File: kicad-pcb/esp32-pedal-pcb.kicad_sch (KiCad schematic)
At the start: 42 parts, among them J1 USB_C_Receptacle_USB2.0_14P, Q1 Q_PMOS_GSD, U1 MCP73871, U2 TLV75733PDBV, U3 ESP32-S3-WROOM-1, U4 TPD2EUSB30, U5 TPD2E2U06DCK, U6 TPS2553DBVR

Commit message: Update PCB schematic
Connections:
- net GND: now also D2.2 (A2); no longer D2.1 (A1)
- net VBUS PROTECTED: now also D2.1 (A1); no longer D2.2 (A2)
- net BAT SWITCHED renamed 5V SWITCHED
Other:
- moved on the sheet: D2
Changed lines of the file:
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@@
 	)
 	(junction
+		(at 90.17 74.93)
+		(diameter 0)
+		(color 0 0 0 0)
+	)
+	(junction
 		(at 152.4 144.78)
 		(diameter 0)
@@
 	)
 	(junction
-		(at 90.17 74.93)
-		(diameter 0)
-		(color 0 0 0 0)
-	)
-	(junction
 		(at 167.64 116.84)
 		(diameter 0)
@@
 	(wire
 		(pts
-			(xy 90.17 74.93) (xy 93.98 74.93)
-		)
-		(stroke
-			(width 0)
-			(type default)
-		)
-	)
-	(wire
-		(pts
 			(xy 97.79 58.42) (xy 71.12 58.42)
 		)
@@
 	(wire
 		(pts
+			(xy 90.17 74.93) (xy 93.98 74.93)
+		)
+		(stroke
+			(width 0)
+			(type default)
+		)
+	)
+	(wire
+		(pts
 			(xy 265.43 214.63) (xy 265.43 227.33)
 		)
@@
 		)
 	)
-	(label "BAT SWITCHED"
+	(label "5V SWITCHED"
 		(at 182.88 85.09 0)
 		(effects
@@
 	(symbol
 		(lib_id "Diode:SMF5V0A")
-		(at 90.17 78.74 90)
+		(at 90.17 78.74 270)
 		(unit 1)
 		(exclude_from_sim no)
@@
 					(size 1.27 1.27)
 				)
-				(justify right)
+				(justify left)
 			)
 		)
@@
 					(size 1.27 1.27)
 				)
-				(justify right)
+				(justify left)
 			)
 		)
 		(property "Footprint" "Diode_SMD:D_SMF"
-			(at 95.25 78.74 0)
+			(at 85.09 78.74 0)
 			(effects
 				(font
@@
 		)
 		(property "Datasheet" "https://www.vishay.com/doc?85881"
-			(at 90.17 80.01 0)
+			(at 90.17 77.47 0)
 			(effects
 				(font

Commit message: Update PCB schematic
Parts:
- removed C1: 0.1µF, Capacitor_SMD:C_0805_2012Metric, symbol Device:C_Small_US
- removed C2: 1µF, Capacitor_SMD:C_0805_2012Metric, symbol Device:C_US
- removed C3: 47µF, Capacitor_SMD:C_0805_2012Metric, symbol Device:C_US
- removed C4: 100µF, Capacitor_SMD:C_0805_2012Metric, symbol Device:C_US
- removed C5: 0.1µF, Capacitor_SMD:C_0805_2012Metric, symbol Device:C_US
- removed C6: 1µF, Capacitor_SMD:C_0805_2012Metric, symbol Device:C_Small_US
- removed C7: 10µF, Capacitor_SMD:C_0805_2012Metric, symbol Device:C_Small_US
- added C2, C5: 47µF, Capacitor_SMD:C_0603_1608Metric, symbol Device:C_Small
- added C3, C4: 0.1µF, Capacitor_SMD:C_0603_1608Metric, symbol Device:C_Small
- added C7: 1µF, Capacitor_SMD:C_0603_1608Metric, symbol Device:C_Small
- added C8: 100µF, Capacitor_SMD:C_0603_1608Metric, symbol Device:C_Small
- added C9: 10µF, Capacitor_SMD:C_0603_1608Metric, symbol Device:C_Small
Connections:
- net 3V3: now also C8.1
- net GND: now also C4.1, C7.1
- net RESET: now also C7.2
- net VBUS PROTECTED: now also C2.1, C9.2
- net at U1.18 (IN), U1.19 (IN): now also C2.2
- net MCP OUT: now reaches R5.2, U1.1 (OUT), U1.20 (OUT)
- net MCP OUT: now also C5.2
- net at U3.2 (3V3): now also C8.2
- net at TP1.1: now also C5.1
- net at U1.2 (VPCC): now also C3.2
- net at R9.1: now also C4.2
- new net: C3.1, C9.1

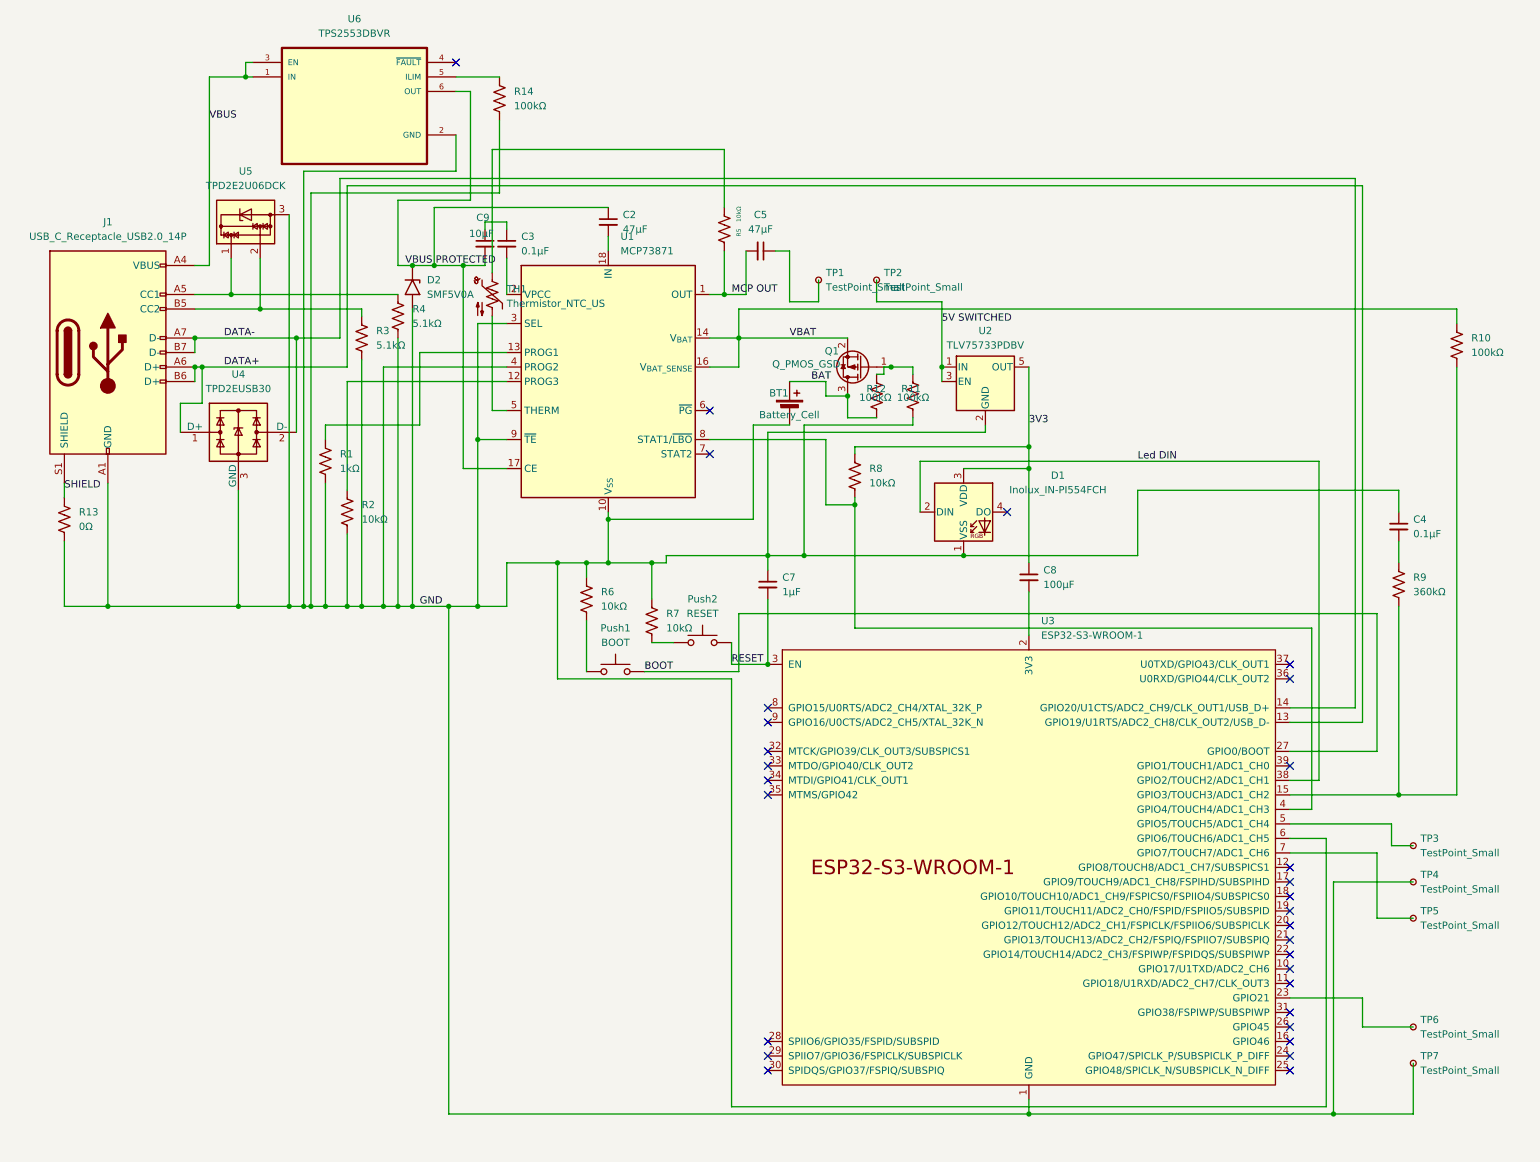
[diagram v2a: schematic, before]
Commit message: Update PCB schematic and layout files
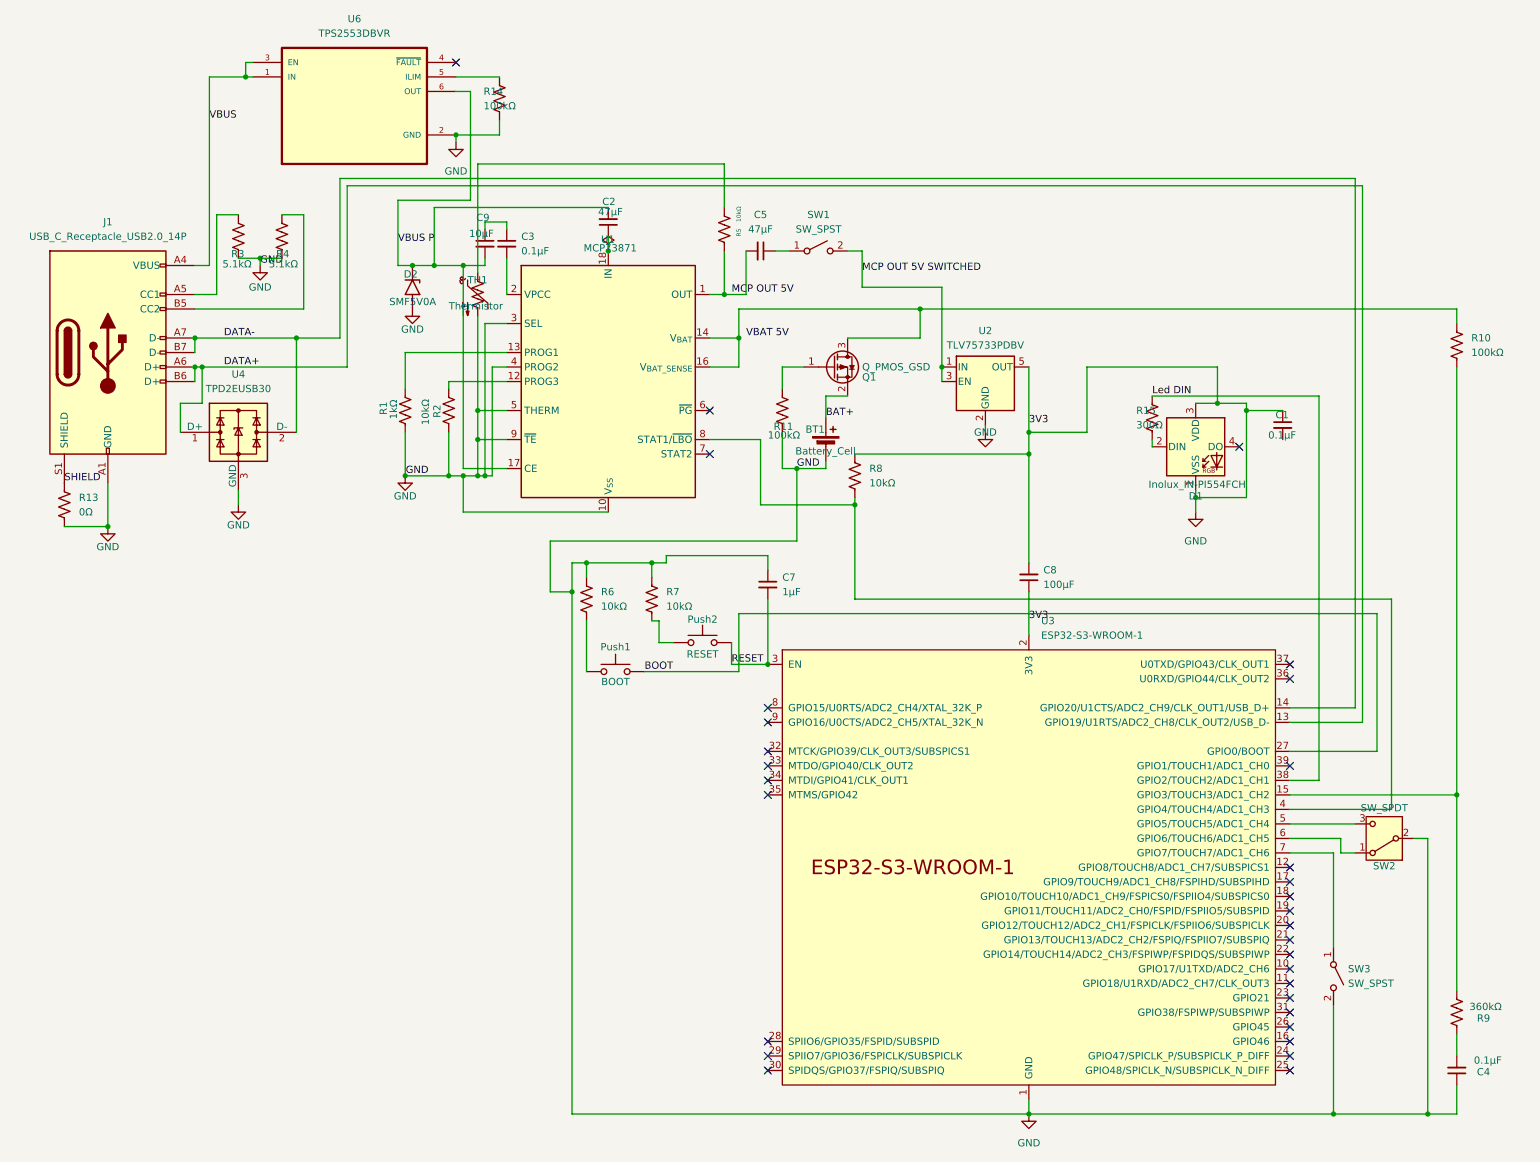
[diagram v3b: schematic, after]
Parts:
- removed R12: 100kΩ, Resistor_SMD:R_0603_1608Metric, symbol Device:R_US
- removed TP1, TP2, TP3, TP4, TP5, TP6, TP7: TestPoint_Small, TestPoint_THTPad_D2.0mm_Drill1.0mm, symbol Connector:TestPoint_Small
- removed U5: TPD2E2U06DCK, Package_TO_SOT_SMD:SOT-323_SC-70, symbol Power_Protection:TPD2E2U06DCK
- added C1: 0.1µF, Capacitor_SMD:C_0603_1608Metric, symbol Device:C_Small
- added R15: 300Ω, Resistor_SMD:R_0603_1608Metric, symbol Device:R_US
- added SW1, SW3: SW_SPST, Connector_Wire:SolderWire-0.1sqmm_1x02_P3.6mm_D0.4mm_OD1mm, symbol Switch:SW_SPST
- added SW2: SW_SPDT, Connector_Wire:SolderWire-0.1sqmm_1x03_P3.6mm_D0.4mm_OD1mm, symbol Switch:SW_SPDT
- TH1: value Thermistor_NTC_US -> Thermistor; footprint Connector_Wire:SolderWire-0.5sqmm_1x02_P4.6mm_D0.9mm_OD2.1mm -> Connector_Wire:SolderWire-0.1sqmm_1x02_P3.6mm_D0.4mm_OD1mm
- U6: symbol Cossin:TPS2553DBVR -> TPS2553:TPS2553DBVR
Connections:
- net 3V3 is gone; now on net GND: C8.1, D1.3 (VDD), R8.1, U2.5 (OUT)
- net GND: now also C8.2, TH1.2, U1.5 (THERM), U3.2 (3V3), C1.1, SW2.2 (B), SW3.2 (B); no longer U3.6 (GPIO6/TOUCH6/ADC1_CH5)
- net Led DIN: now also R15.1; no longer D1.2 (DIN)
- net at J1.A5 (CC1): now also R3.1; no longer R4.1
- net at J1.B5 (CC2): now also R4.1; no longer R3.1
- net at U1.18 (IN), U1.19 (IN): now also C2.1; no longer C2.2
- net at U3.5 (GPIO5/TOUCH5/ADC1_CH4): now also SW2.3 (C)
- net at U3.7 (GPIO7/TOUCH7/ADC1_CH6): now also SW3.1 (A)
- net at C5.1: now also SW1.1 (A)
- net 5V SWITCHED renamed MCP OUT 5V SWITCHED
- net MCP OUT 5V SWITCHED: now also SW1.2 (B)
- net BAT: no longer names the net of Q1.3 (D)
- net BAT: now also R10.1, U1.14 (V_{BAT}), U1.15 (V_{BAT}), U1.16 (V_{BAT_SENSE}); no longer BT1.1 (+)
- net MCP OUT renamed MCP OUT 5V
- removed net VBAT: Q1.2 (S), R10.1, U1.14 (V_{BAT}), U1.15 (V_{BAT}), U1.16 (V_{BAT_SENSE})
- net VBUS PROTECTED renamed VBUS P
- net VBUS P: now also C2.2; no longer C2.1
- new net: SW2.1 (A), U3.6 (GPIO6/TOUCH6/ADC1_CH5)
- new net: D1.2 (DIN), R15.2
- new net BAT+: BT1.1 (+), Q1.2 (S)
- no-connect marks 30 -> 31
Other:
- moved on the sheet: BT1, C2, C4, C8, D1, Q1, R1, R11, R13, R2, R3, R4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
